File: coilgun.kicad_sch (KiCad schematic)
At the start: 35 parts, among them J1 Conn_01x02, J2 Conn_02x05_Odd_Even, J3 Conn_02x05_Odd_Even, J4 Conn_01x03, J5 Conn_01x03, J6 Conn_01x02, J7 Conn_01x02, J8 Conn_01x02, Q1 BC547, U1 4082, U2 LM555xN, U3 FAN3122xMX, U4 L7815, U5 L7805

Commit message: Route pcb
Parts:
- added C14: 100nF, Capacitor_THT:C_Rect_L7.0mm_W2.0mm_P5.00mm, symbol Device:C
- added D3, D4: LED, LED_THT:LED_D5.0mm, symbol Device:LED
- added Q2: BC558, Package_TO_SOT_THT:TO-92_HandSolder, symbol Transistor_BJT:BC558
- added R6, R7, R8, R9: R, Resistor_THT:R_Axial_DIN0309_L9.0mm_D3.2mm_P15.24mm_Horizontal, symbol Device:R
- C7: footprint Capacitor_THT:CP_Radial_D10.0mm_P5.00mm_P7.50mm -> Capacitor_THT:C_Rect_L7.0mm_W2.0mm_P5.00mm
- J4, J5: footprint Connector_JST:JST_NV_B03P-NV_1x03_P5.00mm_Vertical -> Connector_PinHeader_2.54mm:PinHeader_1x03_P2.54mm_Vertical
- Q1: footprint Package_TO_SOT_THT:TO-92_Inline -> Package_TO_SOT_THT:TO-92_HandSolder
- RV1: footprint Potentiometer_THT:Potentiometer_ACP_CA14V-15_Vertical_Hole -> Potentiometer_THT:Potentiometer_Bourns_3386P_Vertical
- U2: footprint Package_DIP:DIP-8_W7.62mm -> Package_DIP:DIP-8_W7.62mm_Socket_LongPads
- U3: footprint Package_SO:SOIC-8_3.9x4.9mm_P1.27mm -> Package_DIP:DIP-8_W7.62mm_Socket_LongPads
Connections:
- net +5V: now also J2.3 (Pin_3), J3.3 (Pin_3)
- net FIRE_PIN: now also R6.1
- net GND: now also C14.2, D3.1 (K), Q2.1 (C)
- net SAFETY: now also R7.1
- net VDD: now also C14.1, D4.2 (A); no longer J2.3 (Pin_3), J3.3 (Pin_3)
- net at U1.1, U1.9: now also R9.1; no longer Q1.2 (B)
- new net: Q2.2 (B), R7.2
- new net: Q2.3 (E), R8.2
- new net: D4.1 (K), R8.1
- new net: Q1.2 (B), R9.2
- new net: D3.2 (A), R6.2

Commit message: Add values to elements
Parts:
- C1: value C -> 10nF
- C2: now not fitted
- C3: value C_Polarized -> 1uF
- C4, C5, C6: value C -> 100nF
- C7: value C_Polarized -> 10uF Tantal
- D1: value D_Schottky -> 1n5819
- R1, R4, R5, R7: value R -> 10K
- R2, R3: value R -> 10R
- RV1: value R_Potentiometer -> 100K
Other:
- moved on the sheet: C7
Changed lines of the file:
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@@
 	(wire
 		(pts
-			(xy 99.06 168.91) (xy 82.55 168.91)
-		)
-		(stroke
-			(width 0)
-			(type default)
-		)
-	)
-	(wire
-		(pts
 			(xy 49.53 130.81) (xy 49.53 125.73)
 		)
@@
 	(wire
 		(pts
-			(xy 27.94 157.48) (xy 27.94 168.91)
+			(xy 25.4 157.48) (xy 25.4 168.91)
 		)
 		(stroke
@@
 	(wire
 		(pts
+			(xy 80.01 168.91) (xy 99.06 168.91)
+		)
+		(stroke
+			(width 0)
+			(type default)
+		)
+	)
+	(wire
+		(pts
 			(xy 153.67 118.11) (xy 168.91 118.11)
 		)
@@
 	(wire
 		(pts
-			(xy 82.55 157.48) (xy 82.55 168.91)
+			(xy 80.01 157.48) (xy 80.01 168.91)
 		)
 		(stroke
@@
 	(wire
 		(pts
-			(xy 44.45 168.91) (xy 27.94 168.91)
+			(xy 251.46 148.59) (xy 251.46 138.43)
 		)
 		(stroke
@@
 	(wire
 		(pts
-			(xy 251.46 148.59) (xy 251.46 138.43)
+			(xy 168.91 137.16) (xy 168.91 143.51)
 		)
 		(stroke
@@
 	(wire
 		(pts
-			(xy 168.91 137.16) (xy 168.91 143.51)
+			(xy 72.39 171.45) (xy 57.15 171.45)
 		)
 		(stroke
@@
 	(wire
 		(pts
-			(xy 72.39 171.45) (xy 57.15 171.45)
+			(xy 25.4 168.91) (xy 44.45 168.91)
 		)
 		(stroke
@@
 			)
 		)
-		(property "Value" "C_Polarized"
+		(property "Value" "1uF"
 			(at 177.8 84.2009 0)
 			(effects
@@
 			)
 		)
-		(property "Value" "R"
+		(property "Value" "10K"
 			(at 116.84 60.9599 0)
 			(effects
@@
 			)
 		)
-		(property "Value" "C"
+		(property "Value" "100nF"
 			(at 219.71 118.1099 0)
 			(effects
@@
 			)
 		)
-		(property "Value" "C"
+		(property "Value" "100nF"
 			(at 143.51 30.4799 0)
 			(effects
@@
 			)
 		)
-		(property "Value" "R"
+		(property "Value" "10K"
 			(at 218.44 29.2099 0)
 			(effects
@@
 			)
 		)
-		(property "Value" "R"
+		(property "Value" "10K"
 			(at 248.92 92.71 90)
 			(effects
@@
 			)
 		)
-		(property "Value" "R_Potentiometer"
+		(property "Value" "100K"
 			(at 166.37 57.1499 0)
 			(effects
@@
 	(symbol
 		(lib_id "power:VDD")
-		(at 224.79 113.03 0)
+		(at 228.6 113.03 0)
 		(unit 1)
 		(exclude_from_sim no)
@@
 		(fields_autoplaced yes)
 		(property "Reference" "#PWR021"
-			(at 224.79 116.84 0)
+			(at 228.6 116.84 0)
 			(effects
 				(font
@@
 		)
 		(property "Value" "VDD"
-			(at 224.79 107.95 0)
+			(at 228.6 107.95 0)
 			(effects
 				(font
@@
 		)
 		(property "Footprint" ""
-			(at 224.79 113.03 0)
+			(at 228.6 113.03 0)
 			(effects
 				(font
@@
 		)
 		(property "Datasheet" ""
-			(at 224.79 113.03 0)
+			(at 228.6 113.03 0)
 			(effects
 				(font
@@
 		)
 		(property "Description" "Power symbol creates a global label with name \"VDD\""
-			(at 224.79 113.03 0)
+			(at 228.6 113.03 0)
 			(effects
 				(font
@@
 	(symbol
 		(lib_id "Device:C_Polarized")
-		(at 224.79 116.84 0)
+		(at 228.6 116.84 0)
 		(unit 1)
 		(exclude_from_sim no)
@@
 		(fields_autoplaced yes)
 		(property "Reference" "C7"
-			(at 228.6 114.6809 0)
+			(at 232.41 114.6809 0)
 			(effects
 				(font
@@
 			)
 		)
-		(property "Value" "C_Polarized"
-			(at 228.6 117.2209 0)
+		(property "Value" "10uF Tantal"
+			(at 232.41 117.2209 0)
 			(effects
 				(font
@@
 		)
 		(property "Footprint" "Capacitor_THT:C_Rect_L7.0mm_W2.0mm_P5.00mm"
-			(at 225.7552 120.65 0)
+			(at 229.5652 120.65 0)
 			(effects
 				(font
@@
 		)
 		(property "Datasheet" "~"
-			(at 224.79 116.84 0)
+			(at 228.6 116.84 0)
 			(effects
 				(font
@@
 		)
 		(property "Description" "Polarized capacitor"
-			(at 224.79 116.84 0)
+			(at 228.6 116.84 0)
 			(effects
 				(font
@@
 			)
 		)
-		(property "Value" "C"
+		(property "Value" "100nF"
 			(at 78.74 58.4199 0)
 			(effects
@@
 			)
 		)
-		(property "Value" "R"
+		(property "Value" "10K"
 			(at 254 29.2099 0)
 			(effects
@@
 			)
 		)
-		(property "Value" "C"
+		(property "Value" "10nF"
 			(at 130.81 85.0899 0)
 			(effects
@@
 			)
 		)
-		(property "Value" "R"
+		(property "Value" "10R"
 			(at 236.22 132.08 90)
 			(effects
@@
 			)
 		)
-		(property "Value" "R"
+		(property "Value" "10R"
 			(at 242.57 142.494 90)
 			(effects
@@
 			)
 		)
-		(property "Value" "D_Schottky"
+		(property "Value" "1n5819"
 			(at 230.886 143.256 0)
 			(effects
@@
 	(symbol
 		(lib_id "power:VDD")
-		(at 82.55 157.48 0)
+		(at 80.01 157.48 0)
 		(unit 1)
 		(exclude_from_sim no)
@@
 		(fields_autoplaced yes)
 		(property "Reference" "#PWR026"
-			(at 82.55 161.29 0)
+			(at 80.01 161.29 0)
 			(effects
 				(font
@@
 		)
 		(property "Value" "VDD"
-			(at 82.55 152.4 0)
+			(at 80.01 152.4 0)
 			(effects
 				(font
@@
 		)
 		(property "Footprint" ""
-			(at 82.55 157.48 0)
+			(at 80.01 157.48 0)
 			(effects
 				(font
@@
 		)
 		(property "Datasheet" ""
-			(at 82.55 157.48 0)
+			(at 80.01 157.48 0)
 			(effects
 				(font
@@
 		)
 		(property "Description" "Power symbol creates a global label with name \"VDD\""
-			(at 82.55 157.48 0)
+			(at 80.01 157.48 0)
 			(effects
 				(font
@@
 	(symbol
 		(lib_id "power:GND")
-		(at 224.79 120.65 0)
+		(at 228.6 120.65 0)
 		(unit 1)
 		(exclude_from_sim no)
@@
 		(fields_autoplaced yes)
 		(property "Reference" "#PWR020"
-			(at 224.79 127 0)
+			(at 228.6 127 0)
 			(effects
 				(font
@@
 		)
 		(property "Value" "GND"
-			(at 224.79 125.73 0)
+			(at 228.6 125.73 0)
 			(effects
 				(font
@@
 		)
 		(property "Footprint" ""
-			(at 224.79 120.65 0)
+			(at 228.6 120.65 0)
 			(effects
 				(font
@@
 		)
 		(property "Datasheet" ""
-			(at 224.79 120.65 0)
+			(at 228.6 120.65 0)
 			(effects
 				(font
@@
 		)
 		(property "Description" "Power symbol creates a global label with name \"GND\" , ground"
-			(at 224.79 120.65 0)
+			(at 228.6 120.65 0)
 			(effects
 				(font
@@
 	(symbol
 		(lib_id "power:VDD")
-		(at 27.94 157.48 0)
+		(at 25.4 157.48 0)
 		(unit 1)
 		(exclude_from_sim no)
@@
 		(fields_autoplaced yes)
 		(property "Reference" "#PWR024"
-			(at 27.94 161.29 0)
+			(at 25.4 161.29 0)
 			(effects
 				(font
@@
 		)
 		(property "Value" "VDD"
-			(at 27.94 152.4 0)
+			(at 25.4 152.4 0)
 			(effects
 				(font
@@
 		)
 		(property "Footprint" ""
-			(at 27.94 157.48 0)
+			(at 25.4 157.48 0)
 			(effects
 				(font
@@
 		)
 		(property "Datasheet" ""
-			(at 27.94 157.48 0)
+			(at 25.4 157.48 0)
 			(effects
 				(font
@@
 		)
 		(property "Description" "Power symbol creates a global label with name \"VDD\""
-			(at 27.94 157.48 0)
+			(at 25.4 157.48 0)
 			(effects
 				(font
@@
 		(in_bom yes)
 		(on_board yes)
-		(dnp no)
+		(dnp yes)
 		(fields_autoplaced yes)
 		(property "Reference" "C2"

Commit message: Fix bugs and label placement
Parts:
- added C15: 1000uF, Capacitor_THT:CP_Radial_D10.0mm_P5.00mm_P7.50mm, symbol Device:C_Polarized
- R9: value R -> 10K
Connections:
- net +5V: now also C4.1, C5.1, D4.2 (A), J7.1 (Pin_1), J8.1 (Pin_1), R1.1, RV1.2, U1.11, U1.12, U1.14 (Vdd), U1.14 (Vdd), U2.4 (R), U2.8 (VCC), C15.1
- net GND: now also R4.2, R5.2, C15.2; no longer J7.2 (Pin_2), J8.2 (Pin_2)
- net SAFETY: now also J8.2 (Pin_2), R5.1; no longer J8.1 (Pin_1), R5.2
- net TRIGGER: now also J7.2 (Pin_2), R4.1; no longer J7.1 (Pin_1), R4.2
- net VDD: no longer C4.1, C5.1, D4.2 (A), R1.1, R4.1, R5.1, RV1.2, U1.11, U1.12, U1.14 (Vdd), U1.14 (Vdd), U2.4 (R), U2.8 (VCC)
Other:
- moved on the sheet: J7, J8, R4, R5

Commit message: Fix error
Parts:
- removed Q2: BC558, Package_TO_SOT_THT:TO-92_HandSolder, symbol Transistor_BJT:BC558
- added C16: 10uF, Capacitor_THT:CP_Radial_D5.0mm_P2.50mm, symbol Device:C_Polarized
- added C17, C18: 100nF, Capacitor_THT:C_Rect_L7.0mm_W2.0mm_P5.00mm, symbol Device:C
- added H1, H2, H3, H6: MountingHole_Pad, MountingHole:MountingHole_2.2mm_M2_Pad_Via, symbol Mechanical:MountingHole_Pad
- added Q2: BC547, Package_TO_SOT_THT:TO-92_HandSolder, symbol Transistor_BJT:BC547
- added R10: 10K, Resistor_THT:R_Axial_DIN0309_L9.0mm_D3.2mm_P15.24mm_Horizontal, symbol Device:R
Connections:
- net +5V: now also R10.1
- net GND: now also C17.2, C18.2, H1.1, H2.1, H3.1, H6.1, Q2.3 (E)
- net SAFETY: now also C17.1
- net TRIGGER: now also C18.1
- net at Q1.1 (C), R1.2: now also C16.2; no longer U2.2 (TR)
- net at R7.2: now also Q2.2 (B)
- net at R8.2: now also Q2.1 (C)
- new net: C16.1, R10.2, U2.2 (TR)
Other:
- moved on the sheet: C4, J4, J5, Q1, R1, R9, U1A

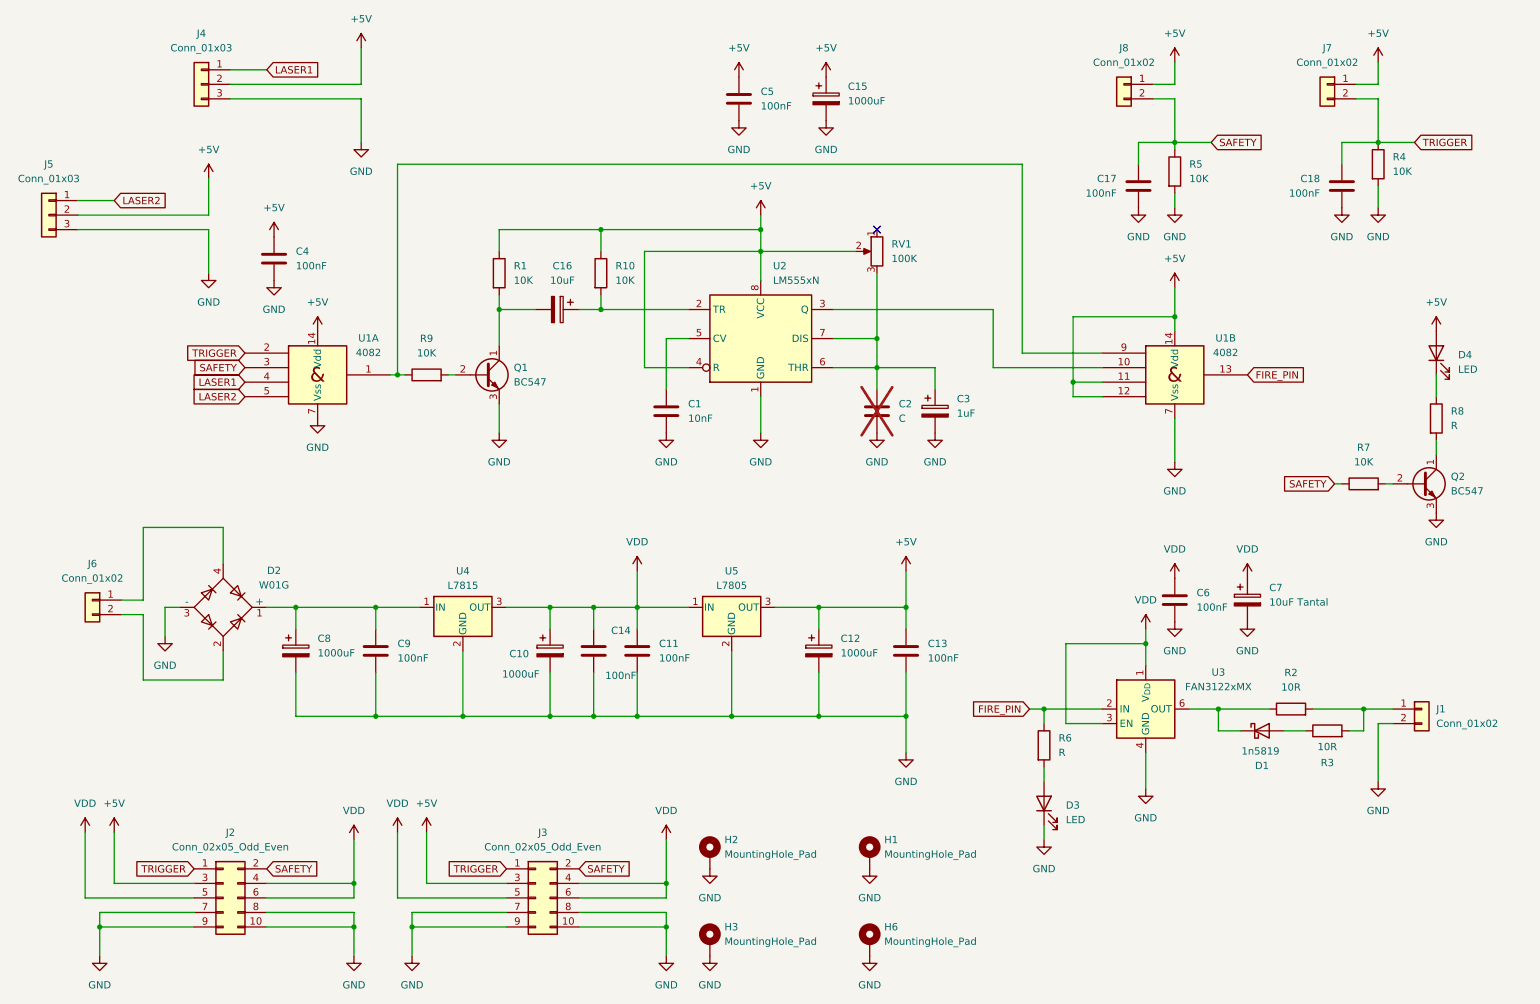
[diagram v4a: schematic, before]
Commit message: safe led, fix 555 trigger, logos
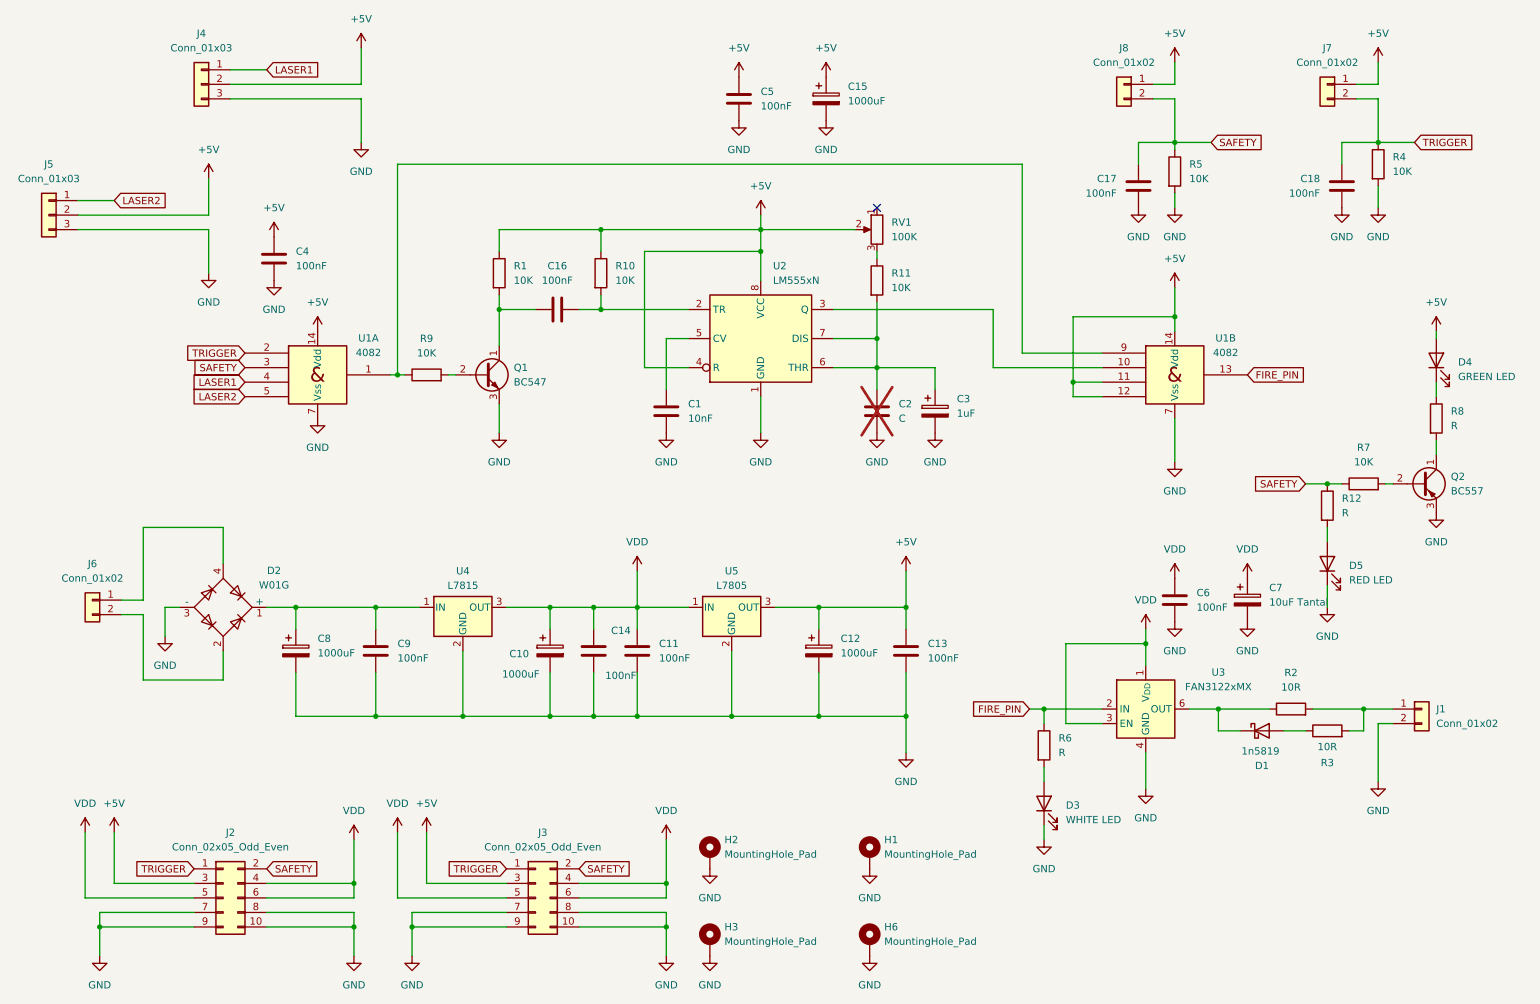
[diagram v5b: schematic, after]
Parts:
- removed C16: 10uF, Capacitor_THT:CP_Radial_D5.0mm_P2.50mm, symbol Device:C_Polarized
- removed Q2: BC547, Package_TO_SOT_THT:TO-92_HandSolder, symbol Transistor_BJT:BC547
- added C16: 100nF, Capacitor_THT:C_Rect_L7.0mm_W2.0mm_P5.00mm, symbol Device:C
- added D5: RED LED, LED_THT:LED_D5.0mm, symbol Device:LED
- added Q2: BC557, Package_TO_SOT_THT:TO-92_HandSolder, symbol Transistor_BJT:BC557
- added R11: 10K, Resistor_THT:R_Axial_DIN0309_L9.0mm_D3.2mm_P15.24mm_Horizontal, symbol Device:R
- added R12: R, Resistor_THT:R_Axial_DIN0309_L9.0mm_D3.2mm_P15.24mm_Horizontal, symbol Device:R
- D3: value LED -> WHITE LED
- D4: value LED -> GREEN LED
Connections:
- net GND: now also D5.1 (K), Q2.3 (E)
- net SAFETY: now also R12.1
- net at R10.2, U2.2 (TR): now also C16.2
- net at C2.1, C3.1, U2.6 (THR)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: now also R11.2; no longer RV1.3
- net at Q1.1 (C), R1.2: now also C16.1
- net at R7.2: now also Q2.2 (B)
- net at R8.2: now also Q2.1 (C)
- new net: R11.1, RV1.3
- new net: D5.2 (A), R12.2
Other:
- moved on the sheet: D4, RV1
